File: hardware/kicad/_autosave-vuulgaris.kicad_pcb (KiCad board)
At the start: 2 copper layers, 284.3 x 125 mm, 69 parts, among them J1 TFPUSH, J10 PJ-603_C41409498, J11 TYPE-C-31-M-12, J2 PJ-376, J3 PJ-376, J4 PJ-376, J5 PJ-376, J7 PJ-603_C41409498, J8 PJ-603_C41409498, J9 PJ-603_C41409498, SW4 CPG151101S03, SW5 CPG151101S03, SW6 CPG151101S03, SW7 CPG151101S03, U1 ES_DAISY_PATCH_SM_REV1, U3 MCP23017-E_SO, U4 MCP23017-E_SO, U5 AMS1117-3.3, U6 AMS1117-3.3, U7 DKM10E-12

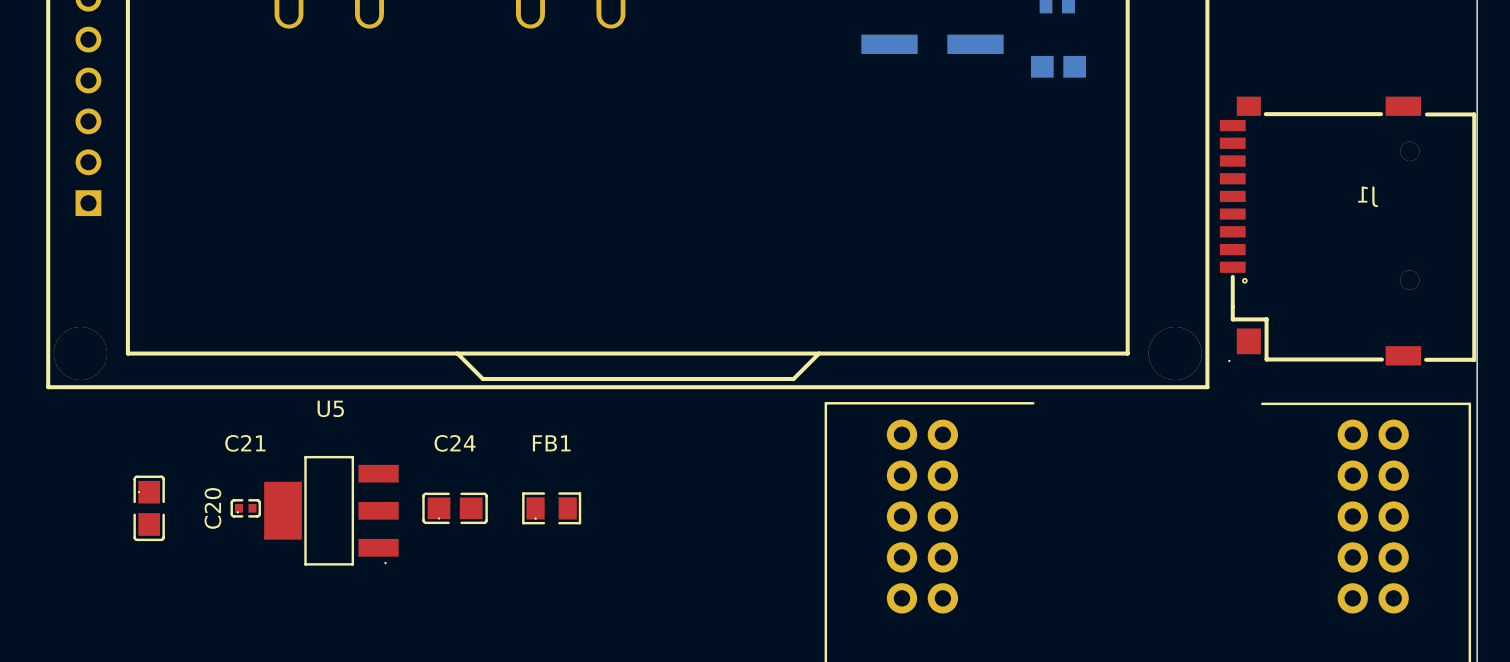
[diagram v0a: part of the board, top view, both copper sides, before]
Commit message: hardware: add SW1/SW2, the two DPDT LPG switches, with a provisional footprint
SW1 is LPG MODE (stereo VCF or stereo VCA), SW2 is SOURCE (resample or external
input). Both DPDT, both pure analog routing on the LPG, both cost zero Daisy
pins. Pins are deliberately unwired until Bergman's circuit is in the repo --
the same treatment RV1-RV4 already get, and the reason netcheck still reports
217/217 with nothing unintended while the component count goes 69 -> 71.

The footprint is PROVISIONAL and marked as such in mksch.py. It is a real,
KiCad-stock, through-hole DPDT -- C&K JS202011CQN -- but it is sub-miniature,
9.5 x 5.2mm with roughly a 2mm actuator, and it will not reach a faceplate
sitting ~10mm above the board. It is there so the parts exist in the schematic
and the netlist; pin count and numbering are identical across DPDTs, so the swap
is one line once the real switch is chosen.

Part selection did not converge and is worth recording rather than repeating.
Every DPDT footprint KiCad ships is a sub-miniature slide switch, none of which
can bridge a panel gap. The right class is a PCB-pin DPDT mini toggle; TE's
MTF206S is exactly that and is out of stock at LCSC. MTS-202 is the most
abundant such switch in the world but is a generic part with no authoritative
datasheet, no KiCad footprint, and none of the sources tried would give a pin
pitch -- only the 6mm panel hole. design-state already warns to verify these
pinouts against the physical part with a meter, so drawing that footprint from a
half-remembered 4.7mm grid is the exact failure this repo keeps having.

Also: place.py stops dropping SW1/SW2 from its panel table once they appear on
the board, so they get faceplate enforcement like every other panel part.

And the micro-USB question is closed -- it exits the RIGHT side of the main PCB,
confirmed against the hardware, which is where U1 already sits. Recorded in
design-state; the carrier footprint still does not mark it.
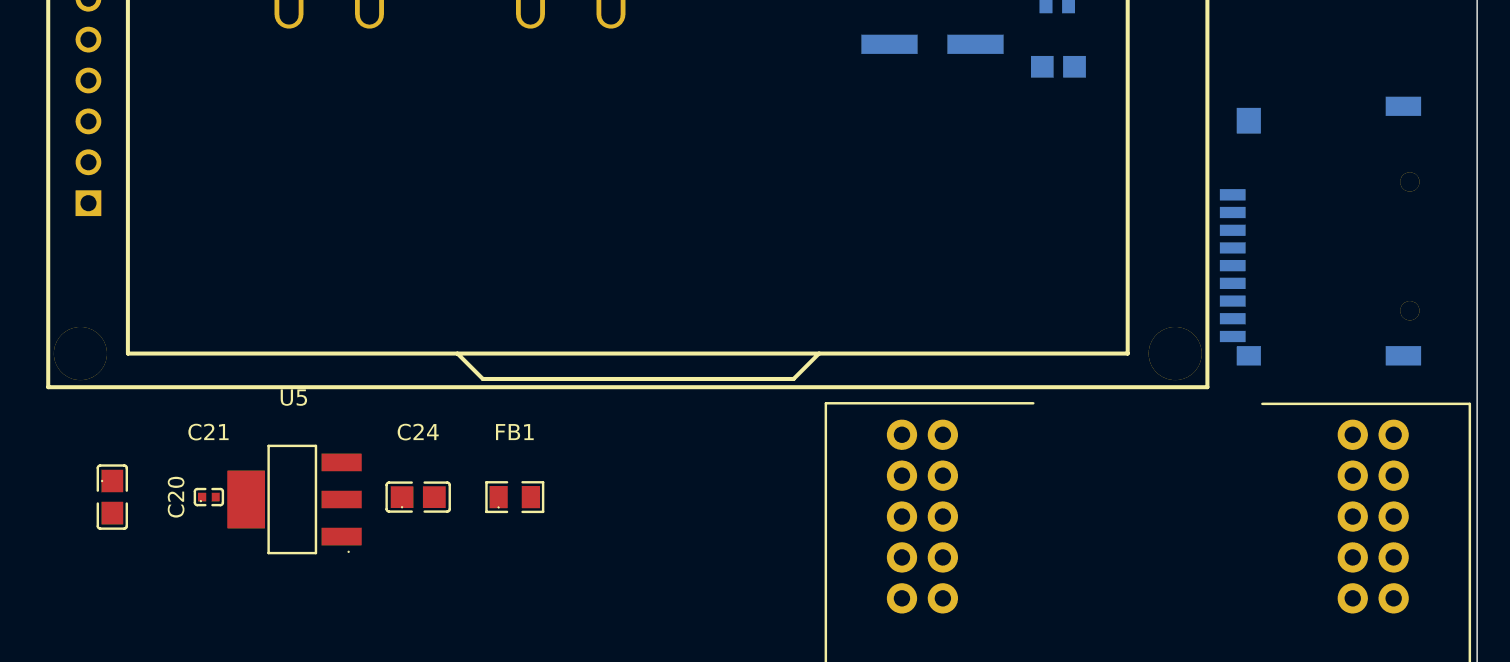
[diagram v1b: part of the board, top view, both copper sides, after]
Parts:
- J1: moved to B.Cu
- moved C20 2.39 mm to (299.5, 103.1)
- moved C21 2.39 mm to (305.5, 103.1)
- moved C24 2.39 mm to (318.5, 103.1)
- moved FB1 2.39 mm to (324.5, 103.1)
- moved U5 2.39 mm to (310.8, 103.2)
- turned J1 to 90 degrees

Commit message: hardware: replace the two DPDT panel toggles with DG419 analog switches
SW1 and SW2 are gone. In their place, U8-U11: four Vishay DG419 SPDT analog
switches, C6581, 2467 in stock. Four SPDT is exactly two DPDT -- U8/U9 are the
MODE switch's L and R poles, U10/U11 the SOURCE switch's -- and sharing one GPIO
per pair gangs them, which is what the mechanical version achieved with a single
actuator. Thrown from MCP23017 U4 GPB3 and GPB4, two of the five spare pins.

This deletes the problem rather than working around it. The blocker was that
every DPDT footprint KiCad ships is a sub-miniature slide switch that cannot
reach a faceplate ~10mm above the board, and the toggles that can are either out
of stock or generic parts with no trustworthy datasheet. None of that matters
now: no actuator, no bushing, no slot, no pinout to confirm with a meter.

It also buys something the toggles could not. Mode and source become software
state, so they recall with the patch, and the Daisy can mute across the
transition instead of letting a hand-thrown contact click into the audio.

DG419 was chosen over the quad parts on availability -- ADG1334 and MAX333A are
the tidier one-package answer but neither is an LCSC line, and this project has
been bitten enough by designing around parts nobody stocks. Break-before-make is
guaranteed, which matters here: these carry audio, and a make-before-break part
would short two sources together during the throw. Pin 5 is a separate logic
supply, tied to P3V3_DAISY so the MCP23017's 3.3V outputs drive it natively.
D/S1/S2 stay unwired until Bergman's circuit lands, as with RV1-RV4.

One trap worth recording. Setting n_switches to 0 made the upper row narrower,
so it re-centred -- every encoder and pot moved 11mm right and RV1's pads went
through J7's. A cosmetic reflow silently breaking a verified layout. Added
switch_reserve_slots, which holds the row where it was; set it to 0 to actually
reclaim the space, deliberately rather than by accident.

255/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
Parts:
- added SW1: SW_DPDT_x2, vuulgaris:SW_CuK_JS202011CQN_DPDT_Straight, F.Cu at (276.4, 92.8)
- added SW2: SW_DPDT_x2, vuulgaris:SW_CuK_JS202011CQN_DPDT_Straight, F.Cu at (282.7, 92.8)
- J1: moved to F.Cu
- moved C27 119.3 mm to (205.0, 113.0)
- moved U4 52.5 mm to (205.0, 105.0), turned to 0 degrees
- moved SW5 8.66 mm to (135.5, 134.3)
- moved SW4 8.66 mm to (116.4, 134.3)
- moved ENC0 8.66 mm to (126.6, 114.1)
- moved SW7 8.66 mm to (135.5, 153.4)
- moved SW6 8.66 mm to (116.4, 153.4)
- moved C20 2.39 mm to (301.8, 103.8)
- moved C21 2.39 mm to (307.8, 103.8)
- moved C24 2.39 mm to (320.8, 103.8)
- moved FB1 2.39 mm to (326.8, 103.8)
- moved U5 2.39 mm to (313.1, 103.9)
- moved ENC10 2.13 mm to (212.1, 84.6)
- moved ENC2 2.13 mm to (118.1, 84.6)
- moved ENC4 2.13 mm to (140.1, 84.6)
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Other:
- board size 284.3 x 125 mm -> 284.3 x 116.8 mm

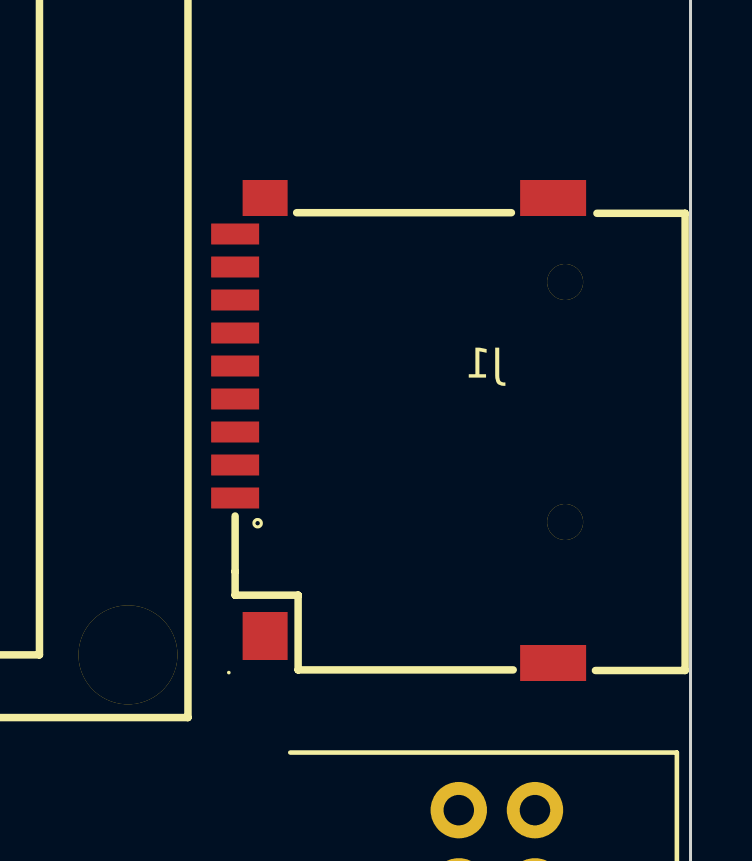
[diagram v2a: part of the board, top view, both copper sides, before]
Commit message: hardware: SW1/SW2 back to mechanical -- Dailywell DW3, footprint from the drawing
Reverts the DG419 analog switches. U8-U11 and their eight decoupling caps are
gone, U4 GPB3/GPB4 are spare again, and SW1/SW2 are mechanical DPDT toggles.

The part is a Dailywell 2MD1T1B1M2QES, DPDT ON-ON, PC pin -- Thonk sell it as
DW3. It is the Eurorack DIY standard, used by Music Thing and Zlob among others,
and Thonk's own note is what settles the question that blocked this all
afternoon: soldered into a PCB these "sit at a height that matches box-style
3.5mm sockets and PCB mounting pots", which is exactly this board's geometry.
That is the reach problem answered by the part rather than worked around.

The footprint is drawn from the manufacturer drawing 2MDP0428 rev C, not from
memory. Fetched the PDF, rendered it, and read the P.C. MOUNTING detail directly:
two columns 5.08mm apart, three pins per column at 2.54mm, 1.09mm holes. Panel
hole 4.95mm, bushing 10-48 UNS-2A x 5.59mm long. The drawing also confirms the
contact table -- POS.1 makes 2-3 and 5-6, POS.3 makes 2-1 and 5-4, so pins 2 and
5 are the commons and the throws are 1/3 and 4/6. design-state predicted exactly
that and told us to verify it rather than assume; now it is verified, and the
note about checking with a meter applies only to substitutes.

The faceplate opening changes with it. It had been a 9 x 20mm vertical SLOT,
which suited a slide actuator; this switch needs a ROUND 4.95mm bushing hole.
switch_w/h stay as the layout footprint the switch occupies in the row so nothing
reflows, and switch_hole_d_mm is what actually gets cut. The stale "switch slots
vertical" check is replaced by one that asserts the hole fits its column.

Pins stay unwired until Bergman's circuit lands, as with RV1-RV4.

217/217 netcheck, faceplate clean, all 20 panel parts on their holes, no
overlaps, Gerbers clean. Board needs F8 to pick up SW1/SW2.
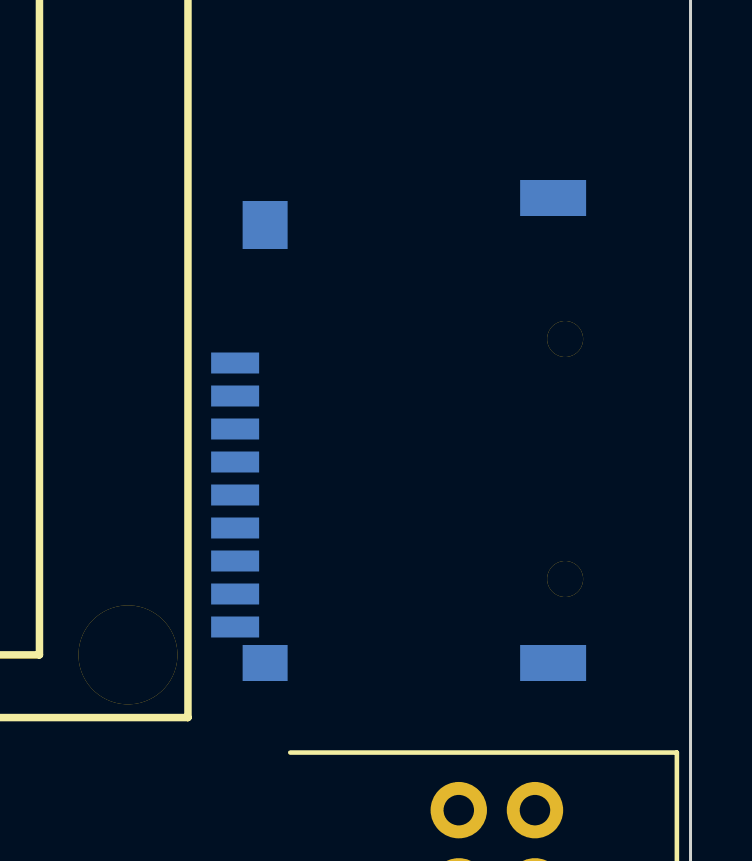
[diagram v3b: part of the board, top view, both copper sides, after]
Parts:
- J1: moved to B.Cu
- turned J1 to 90 degrees
